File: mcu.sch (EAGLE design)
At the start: 63 parts, among them IC1 MCP73831/OT, T1 SI7051-A20, U12 BQ297XY, U4 NRF52832, U7 CP2102N-A01-GQFN24, X1 LFXTAL069526, X6 32.768kHz

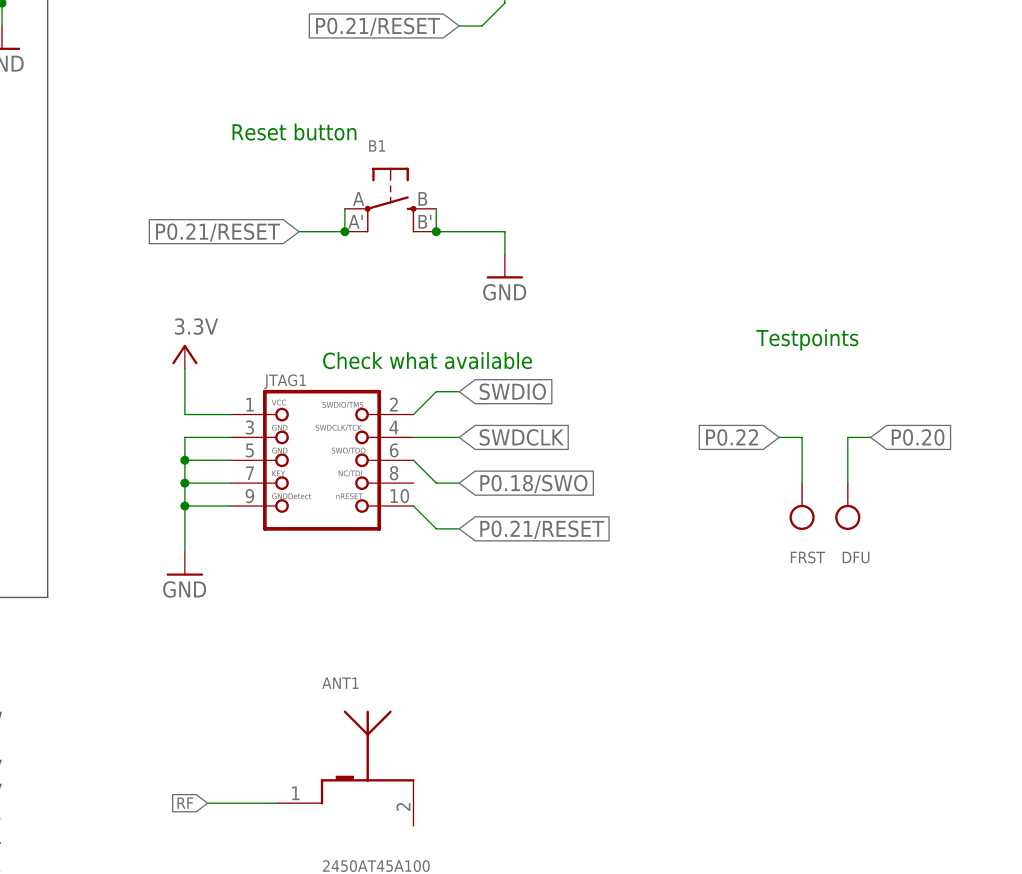
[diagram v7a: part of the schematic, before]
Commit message: UPD: testpoints schematic
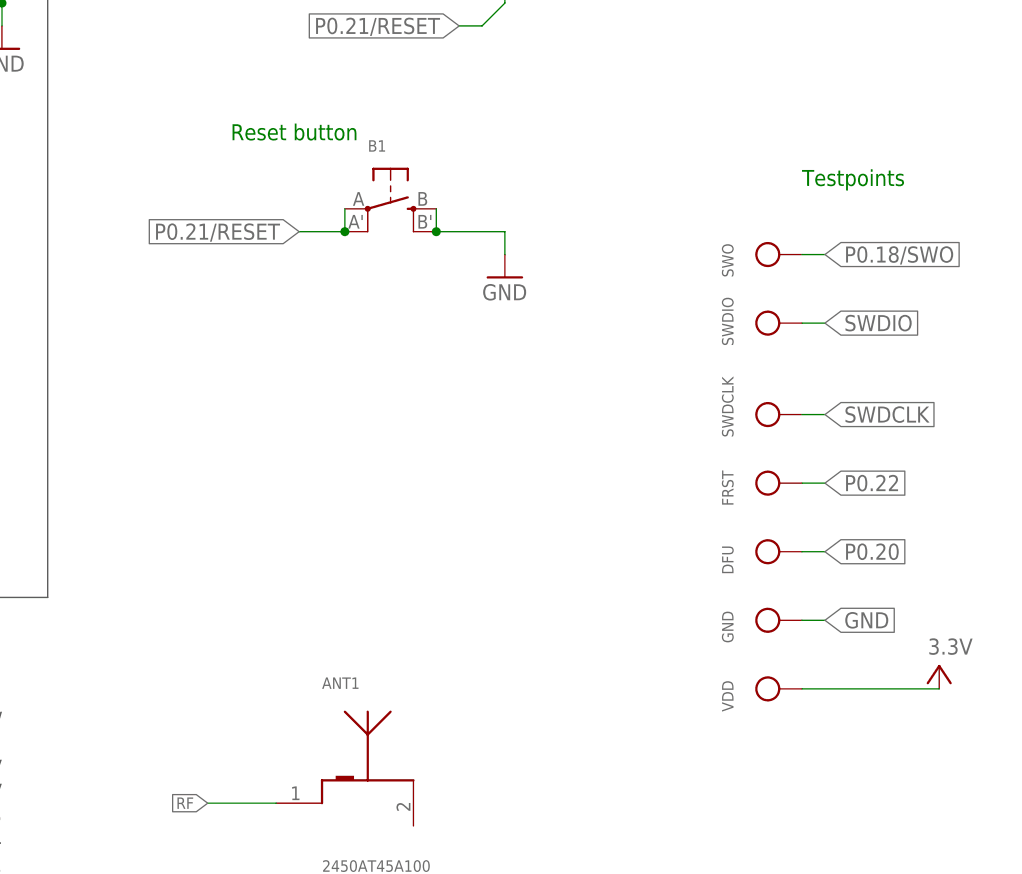
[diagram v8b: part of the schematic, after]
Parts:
- removed JTAG1: (no value), microbuilder:JTAG-CORTEXM3
- added GND, SWDCLK, SWDIO, SWO, VDD: (no value), microbuilder:TESTPOINTROUND2MM
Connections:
- net GND: now also GND.P$1; no longer JTAG1.3, JTAG1.5, JTAG1.7, JTAG1.9
- net P0.18/SWO: now also SWO.P$1; no longer JTAG1.6
- net P0.21/RESET: no longer JTAG1.10
- net SWDCLK: now also SWDCLK.P$1; no longer JTAG1.4
- net SWDIO: now also SWDIO.P$1; no longer JTAG1.2
- net V+: now also VDD.P$1; no longer JTAG1.1
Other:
- note removed: "Check what available"
- moved on the sheet: DFU, FRST
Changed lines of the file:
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@@
 <layer number="18" name="Vias" color="2" fill="1" visible="no" active="no"/>
 <layer number="19" name="Unrouted" color="6" fill="1" visible="no" active="no"/>
-<layer number="20" name="Dimension" color="15" fill="1" visible="no" active="no"/>
-<layer number="21" name="tPlace" color="14" fill="1" visible="no" active="no"/>
-<layer number="22" name="bPlace" color="13" fill="1" visible="no" active="no"/>
-<layer number="23" name="tOrigins" color="14" fill="1" visible="no" active="no"/>
-<layer number="24" name="bOrigins" color="13" fill="1" visible="no" active="no"/>
+<layer number="20" name="Dimension" color="24" fill="1" visible="no" active="no"/>
+<layer number="21" name="tPlace" color="7" fill="1" visible="no" active="no"/>
+<layer number="22" name="bPlace" color="7" fill="1" visible="no" active="no"/>
+<layer number="23" name="tOrigins" color="15" fill="1" visible="no" active="no"/>
+<layer number="24" name="bOrigins" color="15" fill="1" visible="no" active="no"/>
 <layer number="25" name="tNames" color="7" fill="1" visible="no" active="no"/>
 <layer number="26" name="bNames" color="7" fill="1" visible="no" active="no"/>
@@
 <part name="B1" library="microbuilder" deviceset="SWITCH_TACT_SMT" device="4.6X2.8"/>
 <part name="GND11" library="supply1" library_urn="urn:adsk.eagle:library:371" deviceset="GND" device=""/>
-<part name="JTAG1" library="microbuilder" deviceset="JTAG-CORTEXM3" device=""/>
-<part name="GND12" library="supply1" library_urn="urn:adsk.eagle:library:371" deviceset="GND" device=""/>
-<part name="VDD_8" library="supply2" library_urn="urn:adsk.eagle:library:372" deviceset="V+" device="" value="3.3V"/>
 <part name="FRST" library="microbuilder" deviceset="TESTPOINT" device="ROUND2MM"/>
 <part name="DFU" library="microbuilder" deviceset="TESTPOINT" device="ROUND2MM"/>
@@
 <part name="C10" library="rcl" library_urn="urn:adsk.eagle:library:334" deviceset="C-EU" device="C0603K" package3d_urn="urn:adsk.eagle:package:23680/2" value="0.1µF"/>
 <part name="GND18" library="supply1" deviceset="GND" device=""/>
+<part name="SWDCLK" library="microbuilder" deviceset="TESTPOINT" device="ROUND2MM"/>
+<part name="SWDIO" library="microbuilder" deviceset="TESTPOINT" device="ROUND2MM"/>
+<part name="GND" library="microbuilder" deviceset="TESTPOINT" device="ROUND2MM"/>
+<part name="VDD" library="microbuilder" deviceset="TESTPOINT" device="ROUND2MM"/>
+<part name="SWO" library="microbuilder" deviceset="TESTPOINT" device="ROUND2MM"/>
+<part name="VDD_11" library="supply2" library_urn="urn:adsk.eagle:library:372" deviceset="V+" device="" value="3.3V"/>
 </parts>
 <sheets>
@@
 <text x="208.28" y="259.08" size="1.778" layer="91">Auto reset from USB signal</text>
 <text x="195.58" y="220.98" size="1.778" layer="91">Reset button</text>
-<text x="205.74" y="195.58" size="1.778" layer="91">Check what available</text>
-<text x="254" y="198.12" size="1.778" layer="91">Testpoints</text>
+<text x="259.08" y="215.9" size="1.778" layer="91">Testpoints</text>
 <text x="121.92" y="368.3" size="1.778" layer="97">10K  = 100mA</text>
 <text x="121.92" y="365.76" size="1.778" layer="97">5.0K  = 200mA</text>
@@
 <instance part="B1" gate="G$1" x="213.36" y="213.36"/>
 <instance part="GND11" gate="1" x="226.06" y="205.74"/>
-<instance part="JTAG1" gate="G$1" x="205.74" y="180.34"/>
-<instance part="GND12" gate="1" x="190.5" y="172.72"/>
-<instance part="VDD_8" gate="1" x="190.5" y="198.12"/>
-<instance part="FRST" gate="G$1" x="259.08" y="182.88" rot="R180"/>
-<instance part="DFU" gate="G$1" x="264.16" y="182.88" rot="R180"/>
+<instance part="FRST" gate="G$1" x="259.08" y="182.88" rot="R90"/>
+<instance part="DFU" gate="G$1" x="259.08" y="175.26" rot="R90"/>
 <instance part="GND13" gate="1" x="-177.8" y="198.12"/>
 <instance part="U$10" gate="G$1" x="-58.42" y="274.32"/>
@@
 <instance part="C10" gate="G$1" x="40.64" y="99.06"/>
 <instance part="GND18" gate="1" x="40.64" y="88.9" rot="MR0"/>
+<instance part="SWDCLK" gate="G$1" x="259.08" y="190.5" rot="R90"/>
+<instance part="SWDIO" gate="G$1" x="259.08" y="200.66" rot="R90"/>
+<instance part="GND" gate="G$1" x="259.08" y="167.64" rot="R90"/>
+<instance part="VDD" gate="G$1" x="259.08" y="160.02" rot="R90"/>
+<instance part="SWO" gate="G$1" x="259.08" y="208.28" rot="R90"/>
+<instance part="VDD_11" gate="1" x="274.32" y="162.56"/>
 </instances>
 <busses>
@@
 <pinref part="GND11" gate="1" pin="GND"/>
 <wire x1="226.06" y1="210.82" x2="226.06" y2="208.28" width="0.1524" layer="91"/>
-</segment>
-<segment>
-<pinref part="JTAG1" gate="G$1" pin="3"/>
-<wire x1="195.58" y1="187.96" x2="190.5" y2="187.96" width="0.1524" layer="91"/>
-<pinref part="GND12" gate="1" pin="GND"/>
-<wire x1="190.5" y1="187.96" x2="190.5" y2="185.42" width="0.1524" layer="91"/>
-<pinref part="JTAG1" gate="G$1" pin="5"/>
-<wire x1="190.5" y1="185.42" x2="190.5" y2="182.88" width="0.1524" layer="91"/>
-<wire x1="190.5" y1="182.88" x2="190.5" y2="180.34" width="0.1524" layer="91"/>
-<wire x1="190.5" y1="180.34" x2="190.5" y2="175.26" width="0.1524" layer="91"/>
-<wire x1="195.58" y1="185.42" x2="190.5" y2="185.42" width="0.1524" layer="91"/>
-<junction x="190.5" y="185.42"/>
-<pinref part="JTAG1" gate="G$1" pin="7"/>
-<wire x1="195.58" y1="182.88" x2="190.5" y2="182.88" width="0.1524" layer="91"/>
-<junction x="190.5" y="182.88"/>
-<pinref part="JTAG1" gate="G$1" pin="9"/>
-<wire x1="195.58" y1="180.34" x2="190.5" y2="180.34" width="0.1524" layer="91"/>
-<junction x="190.5" y="180.34"/>
 </segment>
 <segment>
@@
 <wire x1="40.64" y1="93.98" x2="40.64" y2="91.44" width="0.1524" layer="91"/>
 </segment>
+<segment>
+<pinref part="GND" gate="G$1" pin="P$1"/>
+<wire x1="259.08" y1="167.64" x2="261.62" y2="167.64" width="0.1524" layer="91"/>
+<label x="261.62" y="167.64" size="1.778" layer="95" xref="yes"/>
+</segment>
 </net>
 <net name="DEC1" class="0">
@@
 </segment>
 <segment>
-<pinref part="JTAG1" gate="G$1" pin="2"/>
-<label x="220.98" y="193.04" size="1.778" layer="95" xref="yes"/>
-<wire x1="215.9" y1="190.5" x2="218.44" y2="193.04" width="0.1524" layer="91"/>
-<wire x1="218.44" y1="193.04" x2="220.98" y2="193.04" width="0.1524" layer="91"/>
+<pinref part="SWDIO" gate="G$1" pin="P$1"/>
+<wire x1="259.08" y1="200.66" x2="261.62" y2="200.66" width="0.1524" layer="91"/>
+<label x="261.62" y="200.66" size="1.778" layer="95" xref="yes"/>
 </segment>
 </net>
@@
 </segment>
 <segment>
-<pinref part="JTAG1" gate="G$1" pin="4"/>
-<wire x1="215.9" y1="187.96" x2="220.98" y2="187.96" width="0.1524" layer="91"/>
-<label x="220.98" y="187.96" size="1.778" layer="95" xref="yes"/>
+<pinref part="SWDCLK" gate="G$1" pin="P$1"/>
+<wire x1="259.08" y1="190.5" x2="261.62" y2="190.5" width="0.1524" layer="91"/>
+<label x="261.62" y="190.5" size="1.778" layer="95" xref="yes"/>
 </segment>
 </net>
@@
 <segment>
 <pinref part="FRST" gate="G$1" pin="P$1"/>
-<wire x1="259.08" y1="182.88" x2="259.08" y2="187.96" width="0.1524" layer="91"/>
-<wire x1="259.08" y1="187.96" x2="256.54" y2="187.96" width="0.1524" layer="91"/>
-<label x="256.54" y="187.96" size="1.778" layer="95" rot="R180" xref="yes"/>
+<wire x1="259.08" y1="182.88" x2="261.62" y2="182.88" width="0.1524" layer="91"/>
+<label x="261.62" y="182.88" size="1.778" layer="95" xref="yes"/>
 </segment>
 </net>
@@
 </segment>
 <segment>
-<pinref part="JTAG1" gate="G$1" pin="6"/>
-<label x="220.98" y="182.88" size="1.778" layer="95" xref="yes"/>
-<wire x1="215.9" y1="185.42" x2="218.44" y2="182.88" width="0.1524" layer="91"/>
-<wire x1="218.44" y1="182.88" x2="220.98" y2="182.88" width="0.1524" layer="91"/>
+<pinref part="SWO" gate="G$1" pin="P$1"/>
+<wire x1="259.08" y1="208.28" x2="261.62" y2="208.28" width="0.1524" layer="91"/>
+<label x="261.62" y="208.28" size="1.778" layer="95" xref="yes"/>
 </segment>
 </net>
@@
 <segment>
 <pinref part="DFU" gate="G$1" pin="P$1"/>
-<wire x1="264.16" y1="182.88" x2="264.16" y2="187.96" width="0.1524" layer="91"/>
-<wire x1="264.16" y1="187.96" x2="266.7" y2="187.96" width="0.1524" layer="91"/>
-<label x="266.7" y="187.96" size="1.778" layer="95" xref="yes"/>
+<wire x1="259.08" y1="175.26" x2="261.62" y2="175.26" width="0.1524" layer="91"/>
+<label x="261.62" y="175.26" size="1.778" layer="95" xref="yes"/>
 </segment>
 </net>
@@
 <junction x="208.28" y="210.82"/>
 <label x="203.2" y="210.82" size="1.778" layer="95" rot="R180" xref="yes"/>
-</segment>
-<segment>
-<pinref part="JTAG1" gate="G$1" pin="10"/>
-<label x="220.98" y="177.8" size="1.778" layer="95" xref="yes"/>
-<wire x1="215.9" y1="180.34" x2="218.44" y2="177.8" width="0.1524" layer="91"/>
-<wire x1="218.44" y1="177.8" x2="220.98" y2="177.8" width="0.1524" layer="91"/>
 </segment>
 </net>
@@
 <wire x1="241.3" y1="248.92" x2="241.3" y2="256.54" width="0.1524" layer="91"/>
 <junction x="241.3" y="248.92"/>
-</segment>
-<segment>
-<pinref part="VDD_8" gate="1" pin="V+"/>
-<wire x1="190.5" y1="195.58" x2="190.5" y2="190.5" width="0.1524" layer="91"/>
-<pinref part="JTAG1" gate="G$1" pin="1"/>
-<wire x1="190.5" y1="190.5" x2="195.58" y2="190.5" width="0.1524" layer="91"/>
 </segment>
 <segment>
@@
 <wire x1="-81.28" y1="124.46" x2="-81.28" y2="129.54" width="0.1524" layer="91"/>
 </segment>
-</net>
+<segment>
+<pinref part="VDD" gate="G$1" pin="P$1"/>
+<pinref part="VDD_11" gate="1" pin="V+"/>
+<wire x1="259.08" y1="160.02" x2="274.32" y2="160.02" width="0.1524" layer="91"/>
+</segment>
+</net>
